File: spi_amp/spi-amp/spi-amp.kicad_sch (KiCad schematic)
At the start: 5 parts, among them J1 IN+, J2 IN-, J3 OUT+, J4 OUT-, U1 LMH6401

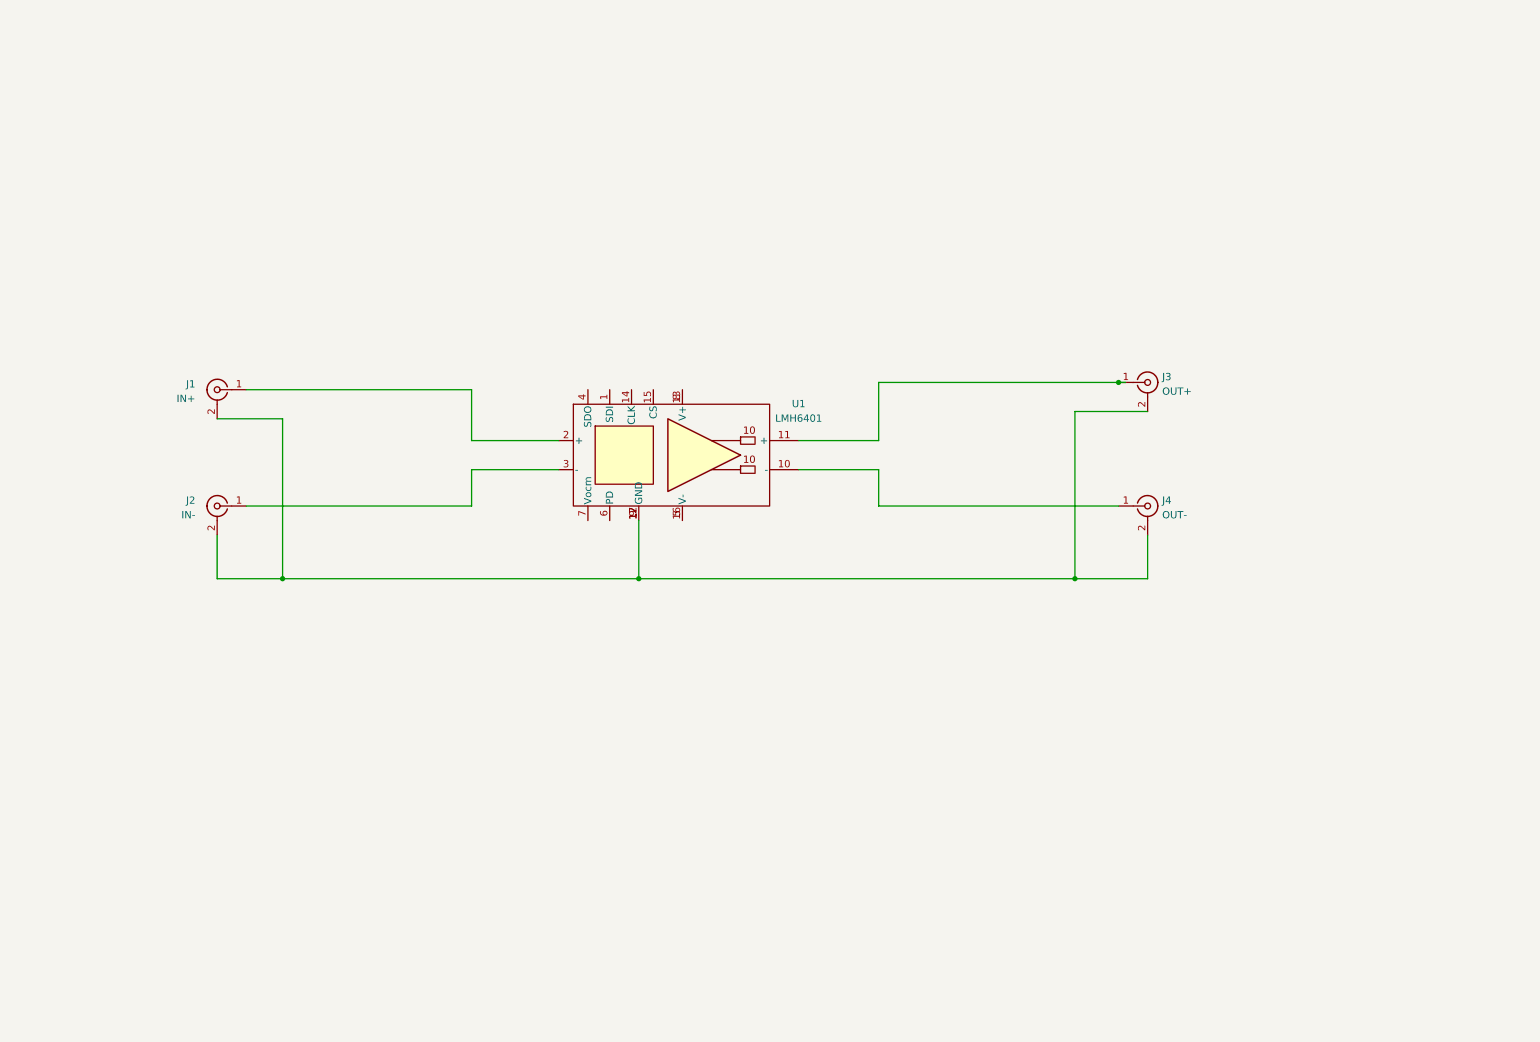
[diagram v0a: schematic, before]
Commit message: Added opto-coupler and voltage regulator.
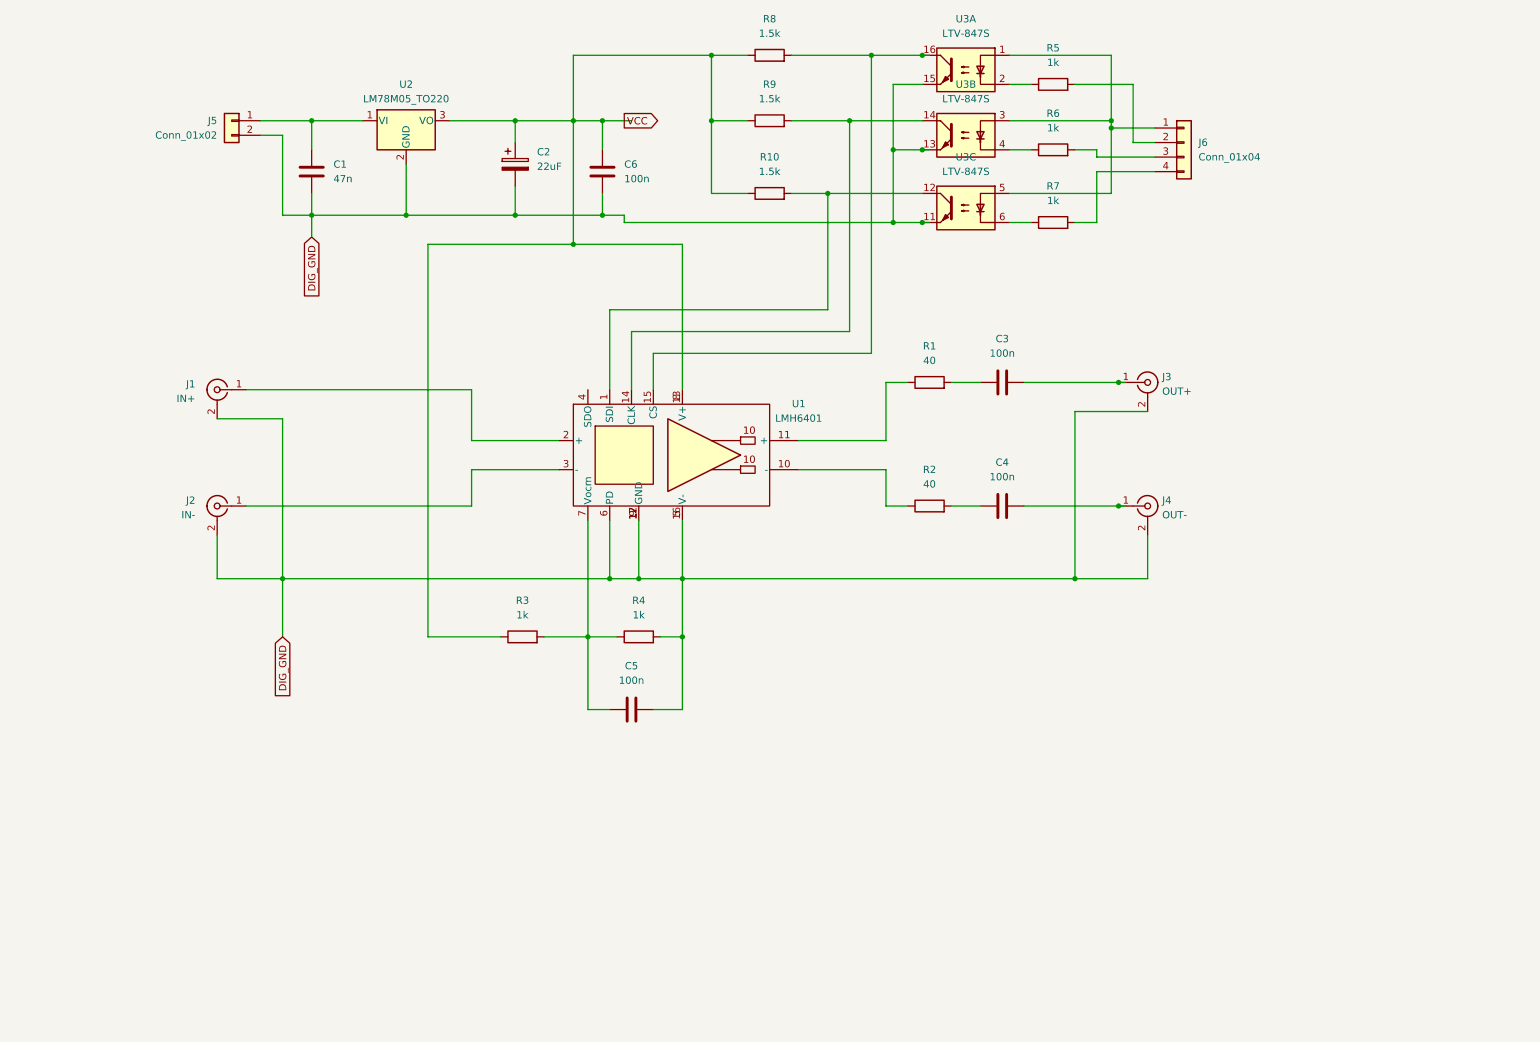
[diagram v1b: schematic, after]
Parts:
- added C1: 47n, Capacitor_THT:C_Disc_D4.3mm_W1.9mm_P5.00mm, symbol Device:C
- added C2: 22uF, Capacitor_THT:CP_Radial_D6.3mm_P2.50mm, symbol Device:C_Polarized
- added C3, C4, C5, C6: 100n, Capacitor_SMD:C_0805_2012Metric_Pad1.18x1.45mm_HandSolder, symbol Device:C
- added J5: Conn_01x02, Connector_PinHeader_2.54mm:PinHeader_1x02_P2.54mm_Vertical, symbol Connector_Generic:Conn_01x02
- added J6: Conn_01x04, Connector_PinSocket_2.54mm:PinSocket_1x04_P2.54mm_Vertical, symbol Connector_Generic:Conn_01x04
- added R1, R2: 40, Resistor_SMD:R_0805_2012Metric_Pad1.20x1.40mm_HandSolder, symbol Device:R
- added R10, R8, R9: 1.5k, Resistor_SMD:R_0805_2012Metric_Pad1.20x1.40mm_HandSolder, symbol Device:R
- added R3, R4, R5, R6, R7: 1k, Resistor_SMD:R_0805_2012Metric_Pad1.20x1.40mm_HandSolder, symbol Device:R
- added U2: LM78M05_TO220, Package_TO_SOT_THT:TO-220-3_Horizontal_TabDown, symbol Regulator_Linear:LM78M05_TO220
- added U3: LTV-847S, Package_DIP:SMDIP-16_W9.53mm, symbol Isolator:LTV-847S
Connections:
- net DIG_GND: now reaches J1.2 (Ext), J2.2 (Ext), J3.2 (Ext), J4.2 (Ext), U1.12 (GND), U1.17 (GND), U1.9 (GND)
- net DIG_GND: now also U1.16 (V-), U1.5 (V-), U1.6 (PD), C1.2, C2.2, C5.2, C6.1, J5.2 (Pin_2), R4.2, U2.2 (GND), U3.11, U3.13, U3.15
- net at U1.1 (SDI): now also R10.2, U3.12
- net at U1.10 (-): now also R2.1; no longer J4.1 (In)
- net at U1.11 (+): now also R1.1; no longer J3.1 (In)
- net VCC: now reaches U1.13 (V+), U1.8 (V+)
- net VCC: now also C2.1, C6.2, R10.1, R3.1, R8.1, R9.1, U2.3 (VO)
- net at U1.14 (CLK): now also R9.2, U3.14
- net at U1.15 (CS): now also R8.2, U3.16
- new net: J6.1 (Pin_1), U3.1, U3.3, U3.5
- new net: R6.1, U3.4
- new net: R5.1, U3.2
- new net: C1.1, J5.1 (Pin_1), U2.1 (VI)
- new net: C5.1, R3.2, R4.1, U1.7 (NC)
- new net: C4.1, R2.2
- new net: C4.2, J4.1 (In)
- new net: R7.1, U3.6
- new net: J6.2 (Pin_2), R5.2
- new net: J6.3 (Pin_3), R6.2
- new net: J6.4 (Pin_4), R7.2
- new net: C3.1, R1.2
- new net: C3.2, J3.1 (In)

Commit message: Fixed layout for SPI RF PCB.
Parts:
- added C7: 100n, Capacitor_SMD:C_0805_2012Metric_Pad1.18x1.45mm_HandSolder, symbol Device:C
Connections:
- net DIG_GND: now also C7.1
- net VCC: now also C7.2
- net LED_VCC: now reaches J6.1 (Pin_1), U3.1, U3.3, U3.5
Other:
- moved on the sheet: C2, C6

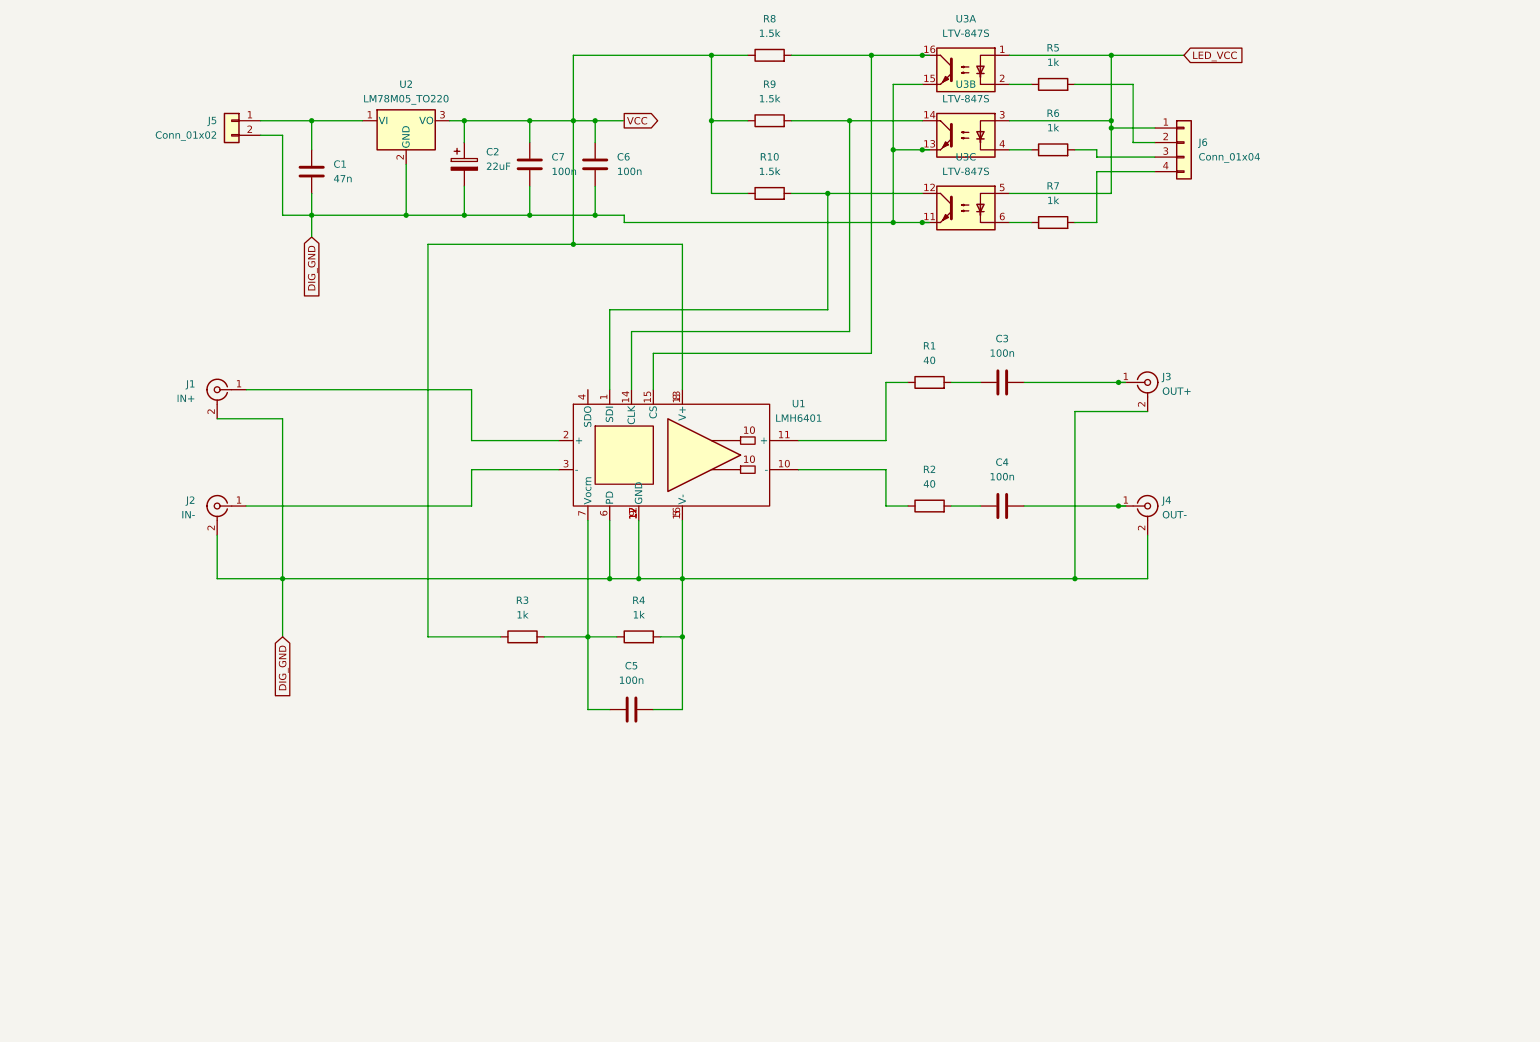
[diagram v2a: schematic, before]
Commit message: Added inverter on input to handle 3.3v.
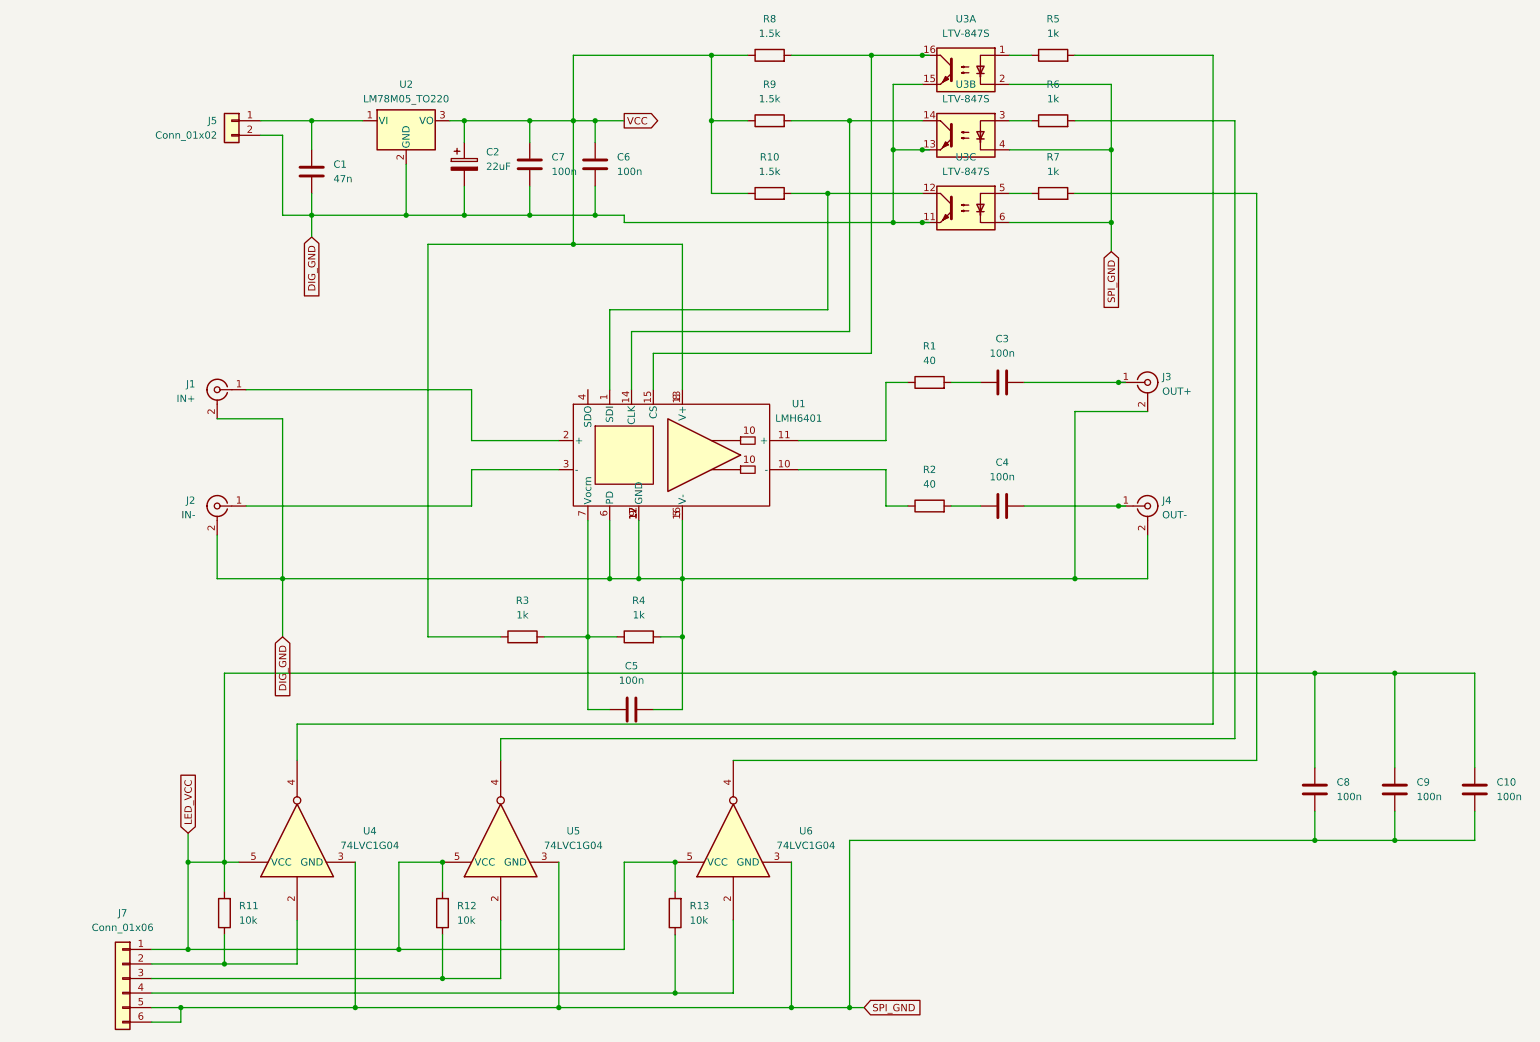
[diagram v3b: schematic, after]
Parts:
- removed J6: Conn_01x04, Connector_PinSocket_2.54mm:PinSocket_1x04_P2.54mm_Vertical, symbol Connector_Generic:Conn_01x04
- added C10, C8, C9: 100n, Capacitor_SMD:C_0805_2012Metric_Pad1.18x1.45mm_HandSolder, symbol Device:C
- added J7: Conn_01x06, Connector_PinHeader_2.54mm:PinHeader_1x06_P2.54mm_Vertical, symbol Connector_Generic:Conn_01x06
- added R11, R12, R13: 10k, Resistor_SMD:R_0805_2012Metric_Pad1.20x1.40mm_HandSolder, symbol Device:R
- added U4, U5, U6: 74LVC1G04, Package_TO_SOT_SMD:SOT-23-5_HandSoldering, symbol 74xGxx:74LVC1G04
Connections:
- net LED_VCC: now also C10.2, C8.2, C9.2, J7.1 (Pin_1), R11.2, R12.2, R13.2, U4.5 (VCC), U5.5 (VCC), U6.5 (VCC); no longer U3.1, U3.3, U3.5
- net at R6.1: now also U3.3; no longer U3.4
- net at R5.1: now also U3.1; no longer U3.2
- net at R7.1: now also U3.5; no longer U3.6
- net at R5.2: now also U4.4
- net at R6.2: now also U5.4
- net at R7.2: now also U6.4
- new net: J7.2 (Pin_2), R11.1, U4.2
- new net: J7.4 (Pin_4), R13.1, U6.2
- new net: J7.3 (Pin_3), R12.1, U5.2
- new net SPI_GND: C10.1, C8.1, C9.1, J7.5 (Pin_5), J7.6 (Pin_6), U3.2, U3.4, U3.6, U4.3 (GND), U5.3 (GND), U6.3 (GND)
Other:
- moved on the sheet: R5, R6, R7

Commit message: Added gerber files and stackup.
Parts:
- C1: value 47n -> 470n
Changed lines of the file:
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@@
 			)
 		)
-		(property "Value" "47n"
+		(property "Value" "470n"
 			(at 67.31 44.4499 0)
 			(show_name no)
